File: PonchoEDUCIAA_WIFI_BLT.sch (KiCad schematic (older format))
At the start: 19 parts, among them J1 UART, U1 ESP32-WROOM

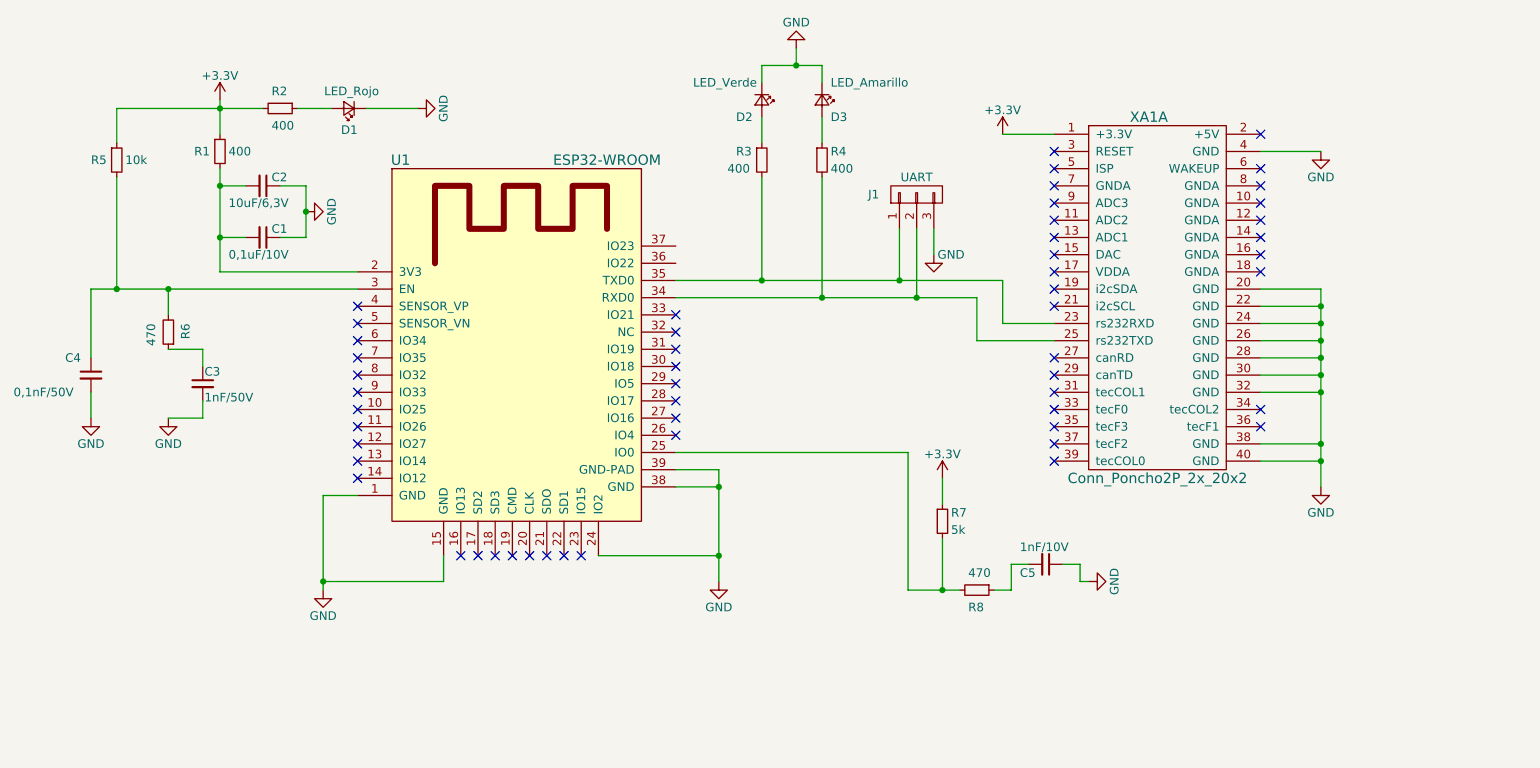
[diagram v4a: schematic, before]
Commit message: Se agregan switches al esquematico
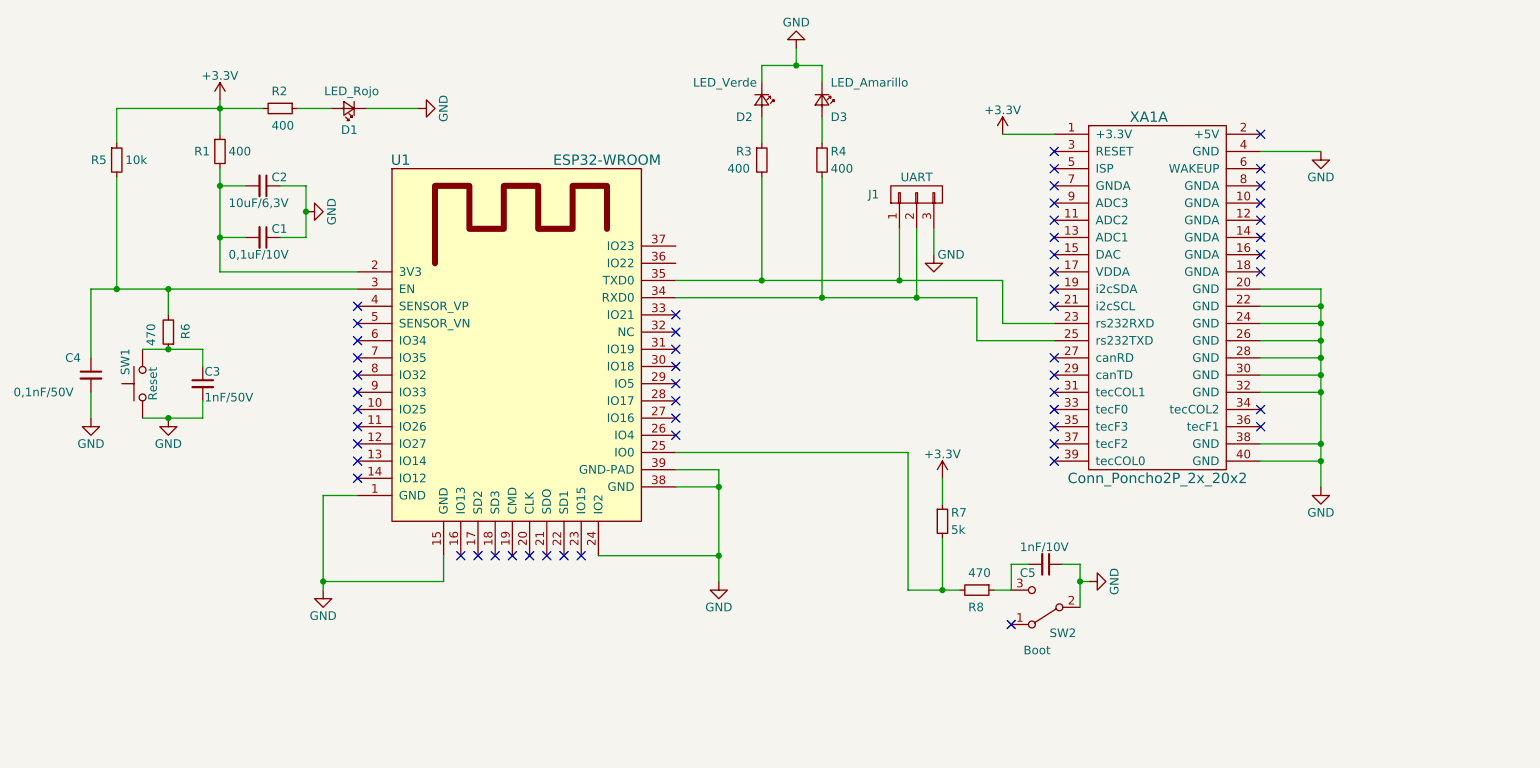
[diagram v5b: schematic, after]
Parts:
- added SW1: Reset, symbol SW_Push
- added SW2: Boot, symbol SW_SPDT
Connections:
- net GND: now also SW1.1, SW2.2 (B)
- net at C3.1, R6.1: now also SW1.2
- net at C5.2, R8.1: now also SW2.3 (C)
- no-connect marks 54 -> 55
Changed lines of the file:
@@
 LIBS:ej2cese
 LIBS:PonchoEDUCIAA_WIFI_BLT
+LIBS:switches
 LIBS:PonchoEDUCIAA_WIFI_BLT-cache
 EELAYER 25 0
@@
 	1    0    0    -1
 $EndComp
-Wire Wire Line
-	4450 5050 4450 5200
-Wire Wire Line
-	4450 5200 3750 5200
-Wire Wire Line
-	3950 4700 3750 4700
-Wire Wire Line
-	3750 4700 3750 5250
-Connection ~ 3750 5200
-Wire Wire Line
-	5800 4650 6050 4650
-Wire Wire Line
-	6050 4550 6050 5200
 $Comp
 L Conn_Poncho2P_2x_20x2 XA1
@@
 	1    0    0    -1
 $EndComp
-Wire Wire Line
-	5800 3550 7550 3550
-Wire Wire Line
-	7550 3550 7550 3800
-Wire Wire Line
-	7550 3800 8000 3800
-Wire Wire Line
-	5800 3450 7700 3450
-Wire Wire Line
-	7700 3450 7700 3700
-Wire Wire Line
-	7700 3700 8000 3700
 $Comp
 L R_Small R1
@@
 	1    0    0    -1
 $EndComp
-Wire Wire Line
-	3950 3400 3150 3400
-Wire Wire Line
-	3150 3400 3150 2800
-Wire Wire Line
-	3150 2400 3150 2600
 $Comp
 L R_Small R3
@@
 	0    1    1    0
 $EndComp
-Wire Wire Line
-	6300 2650 6300 2500
-Wire Wire Line
-	6300 2850 6300 3450
-Connection ~ 6300 3450
 $Comp
 L R_Small R4
@@
 	0    1    1    0
 $EndComp
-Wire Wire Line
-	6650 2650 6650 2500
-Wire Wire Line
-	6300 2300 6300 2200
-Wire Wire Line
-	6300 2200 6650 2200
-Wire Wire Line
-	6500 2200 6500 2100
-Wire Wire Line
-	6650 2200 6650 2300
-Connection ~ 6500 2200
 $Comp
 L R_Small R2
@@
 	0    -1   -1   0
 $EndComp
-Wire Wire Line
-	2550 2450 3400 2450
-Connection ~ 3150 2450
-Wire Wire Line
-	3600 2450 3800 2450
-Wire Wire Line
-	4000 2450 4300 2450
 $Comp
 L +3.3V #PWR?
@@
 	1    0    0    -1
 $EndComp
-Wire Wire Line
-	8000 2600 7700 2600
 $Comp
 L GND #PWR?
@@
 	1    0    0    -1
 $EndComp
-Wire Wire Line
-	9200 2700 9550 2700
 $Comp
 L GND #PWR?
@@
 	1    0    0    -1
 $EndComp
-Wire Wire Line
-	9200 3500 9550 3500
-Wire Wire Line
-	9550 3500 9550 4650
-Wire Wire Line
-	9200 3600 9550 3600
-Connection ~ 9550 3600
-Wire Wire Line
-	9200 3700 9550 3700
-Connection ~ 9550 3700
-Wire Wire Line
-	9200 3800 9550 3800
-Connection ~ 9550 3800
-Wire Wire Line
-	9200 3900 9550 3900
-Connection ~ 9550 3900
-Wire Wire Line
-	9200 4000 9550 4000
-Connection ~ 9550 4000
-Wire Wire Line
-	9200 4100 9550 4100
-Connection ~ 9550 4100
-Wire Wire Line
-	9200 4400 9550 4400
-Connection ~ 9550 4400
-Wire Wire Line
-	9200 4500 9550 4500
-Connection ~ 9550 4500
-Wire Wire Line
-	6650 2850 6650 3550
-Connection ~ 6650 3550
 $Comp
 L CONN_01X03 J1
@@
 	0    -1   -1   0
 $EndComp
-Wire Wire Line
-	7200 3150 7200 3550
-Connection ~ 7200 3550
-Wire Wire Line
-	7100 3150 7100 3450
-Connection ~ 7100 3450
 $Comp
 L GND #PWR?
@@
 	1    0    0    -1
 $EndComp
-Wire Wire Line
-	7300 3300 7300 3150
 $Comp
 L GND #PWR?
@@
 	0    -1   -1   0
 $EndComp
-Wire Wire Line
-	3500 2900 3650 2900
-Wire Wire Line
-	3650 2900 3650 3200
-Wire Wire Line
-	3650 3200 3500 3200
-Connection ~ 3650 3050
-Wire Wire Line
-	3300 2900 3150 2900
-Connection ~ 3150 2900
-Wire Wire Line
-	3300 3200 3150 3200
-Connection ~ 3150 3200
-Wire Wire Line
-	2400 3500 3950 3500
 $Comp
 L R_Small R6
@@
 	-1   0    0    1
 $EndComp
-Wire Wire Line
-	2850 3650 2850 3500
-Connection ~ 2850 3500
-Wire Wire Line
-	3050 3950 3050 3850
-Wire Wire Line
-	3050 3850 2850 3850
-Wire Wire Line
-	2850 4250 3050 4250
-Wire Wire Line
-	3050 4250 3050 4150
 $Comp
 L R_Small R5
@@
 	1    0    0    -1
 $EndComp
-Wire Wire Line
-	2550 2450 2550 2650
-Wire Wire Line
-	2550 3500 2550 2850
 $Comp
 L C_Small C4
@@
 	1    0    0    -1
 $EndComp
-Wire Wire Line
-	2400 3500 2400 3900
-Connection ~ 2550 3500
-Wire Wire Line
-	2400 4100 2400 4250
 NoConn ~ 3950 3600
 NoConn ~ 3950 3700
@@
 NoConn ~ 9200 4200
 NoConn ~ 9200 4300
-Wire Wire Line
-	5800 4450 7150 4450
-Wire Wire Line
-	7150 4450 7150 5250
 $Comp
 L GND #PWR?
@@
 	1    0    0    -1
 $EndComp
-Wire Wire Line
-	7150 5250 7450 5250
-Wire Wire Line
-	7350 5250 7350 4950
-Wire Wire Line
-	7350 4750 7350 4600
 $Comp
 L R_Small R8
@@
 	0    1    1    0
 $EndComp
-Connection ~ 7350 5250
-Wire Wire Line
-	7650 5250 7750 5250
-Wire Wire Line
-	7750 5250 7750 5100
-Wire Wire Line
-	7750 5100 7850 5100
-Wire Wire Line
-	8050 5100 8150 5100
-Wire Wire Line
-	8150 5100 8150 5200
-Wire Wire Line
-	8150 5200 8200 5200
 NoConn ~ 4950 5050
 NoConn ~ 4850 5050
@@
 NoConn ~ 4550 5050
 NoConn ~ 5250 5050
-Wire Wire Line
-	5350 5050 6050 5050
-Connection ~ 6050 5050
 NoConn ~ 5800 3650
 NoConn ~ 5800 3850
@@
 NoConn ~ 3950 4600
 Wire Wire Line
+	4450 5050 4450 5200
+Wire Wire Line
+	4450 5200 3750 5200
+Wire Wire Line
+	3950 4700 3750 4700
+Wire Wire Line
+	3750 4700 3750 5250
+Connection ~ 3750 5200
+Wire Wire Line
+	5800 4650 6050 4650
+Wire Wire Line
+	6050 4550 6050 5200
+Wire Wire Line
+	5800 3550 7550 3550
+Wire Wire Line
+	7550 3550 7550 3800
+Wire Wire Line
+	7550 3800 8000 3800
+Wire Wire Line
+	5800 3450 7700 3450
+Wire Wire Line
+	7700 3450 7700 3700
+Wire Wire Line
+	7700 3700 8000 3700
+Wire Wire Line
+	3950 3400 3150 3400
+Wire Wire Line
+	3150 3400 3150 2800
+Wire Wire Line
+	3150 2400 3150 2600
+Wire Wire Line
+	6300 2650 6300 2500
+Wire Wire Line
+	6300 2850 6300 3450
+Connection ~ 6300 3450
+Wire Wire Line
+	6650 2650 6650 2500
+Wire Wire Line
+	6300 2300 6300 2200
+Wire Wire Line
+	6300 2200 6650 2200
+Wire Wire Line
+	6500 2200 6500 2100
+Wire Wire Line
+	6650 2200 6650 2300
+Connection ~ 6500 2200
+Wire Wire Line
+	2550 2450 3400 2450
+Connection ~ 3150 2450
+Wire Wire Line
+	3600 2450 3800 2450
+Wire Wire Line
+	4000 2450 4300 2450
+Wire Wire Line
+	8000 2600 7700 2600
+Wire Wire Line
+	9200 2700 9550 2700
+Wire Wire Line
+	9200 3500 9550 3500
+Wire Wire Line
+	9550 3500 9550 4650
+Wire Wire Line
+	9200 3600 9550 3600
+Connection ~ 9550 3600
+Wire Wire Line
+	9200 3700 9550 3700
+Connection ~ 9550 3700
+Wire Wire Line
+	9200 3800 9550 3800
+Connection ~ 9550 3800
+Wire Wire Line
+	9200 3900 9550 3900
+Connection ~ 9550 3900
+Wire Wire Line
+	9200 4000 9550 4000
+Connection ~ 9550 4000
+Wire Wire Line
+	9200 4100 9550 4100
+Connection ~ 9550 4100
+Wire Wire Line
+	9200 4400 9550 4400
+Connection ~ 9550 4400
+Wire Wire Line
+	9200 4500 9550 4500
+Connection ~ 9550 4500
+Wire Wire Line
+	6650 2850 6650 3550
+Connection ~ 6650 3550
+Wire Wire Line
+	7200 3150 7200 3550
+Connection ~ 7200 3550
+Wire Wire Line
+	7100 3150 7100 3450
+Connection ~ 7100 3450
+Wire Wire Line
+	7300 3300 7300 3150
+Wire Wire Line
+	3500 2900 3650 2900
+Wire Wire Line
+	3650 2900 3650 3200
+Wire Wire Line
+	3650 3200 3500 3200
+Connection ~ 3650 3050
+Wire Wire Line
+	3300 2900 3150 2900
+Connection ~ 3150 2900
+Wire Wire Line
+	3300 3200 3150 3200
+Connection ~ 3150 3200
+Wire Wire Line
+	2400 3500 3950 3500
+Wire Wire Line
+	2850 3650 2850 3500
+Connection ~ 2850 3500
+Wire Wire Line
+	3050 3850 3050 3950
+Wire Wire Line
+	2700 3850 3050 3850
+Wire Wire Line
+	2700 4250 3050 4250
+Wire Wire Line
+	3050 4250 3050 4150
+Wire Wire Line
+	2550 2450 2550 2650
+Wire Wire Line
+	2550 3500 2550 2850
+Wire Wire Line
+	2400 3500 2400 3900
+Connection ~ 2550 3500
+Wire Wire Line
+	2400 4100 2400 4250
+Wire Wire Line
+	5800 4450 7150 4450
+Wire Wire Line
+	7150 4450 7150 5250
+Wire Wire Line
+	7150 5250 7450 5250
+Wire Wire Line
+	7350 5250 7350 4950
+Wire Wire Line
+	7350 4750 7350 4600
+Connection ~ 7350 5250
+Wire Wire Line
+	7650 5250 7750 5250
+Wire Wire Line
+	7750 5250 7750 5100
+Wire Wire Line
+	7750 5100 7850 5100
+Wire Wire Line
+	8050 5100 8150 5100
+Wire Wire Line
+	8150 5100 8150 5350
+Wire Wire Line
+	8150 5200 8200 5200
+Wire Wire Line
+	5350 5050 6050 5050
+Connection ~ 6050 5050
+Wire Wire Line
 	5800 4550 6050 4550
 Connection ~ 6050 4650
+$Comp
+L SW_Push SW1
+U 1 1 591BAB0F
+P 2700 4050
+F 0 "SW1" H 2750 4150 50  0000 L CNN
+F 1 "Reset" H 2700 3990 50  0000 C CNN
+F 2 "" H 2700 4250 50  0001 C CNN
+F 3 "" H 2700 4250 50  0001 C CNN
+	1    2700 4050
+	0    -1   -1   0
+$EndComp
+Connection ~ 2850 3850
+Connection ~ 2850 4250
+$Comp
+L SW_SPDT SW2
+U 1 1 591BBB9C
+P 7950 5350
+F 0 "SW2" H 7850 5500 50  0000 C CNN
+F 1 "Boot" H 8000 5600 50  0000 C CNN
+F 2 "" H 7950 5350 50  0001 C CNN
+F 3 "" H 7950 5350 50  0001 C CNN
+	1    7950 5350
+	-1   0    0    1
+$EndComp
+Connection ~ 8150 5200
+NoConn ~ 7750 5450
 $EndSCHEMATC

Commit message: Se agregan los footprints
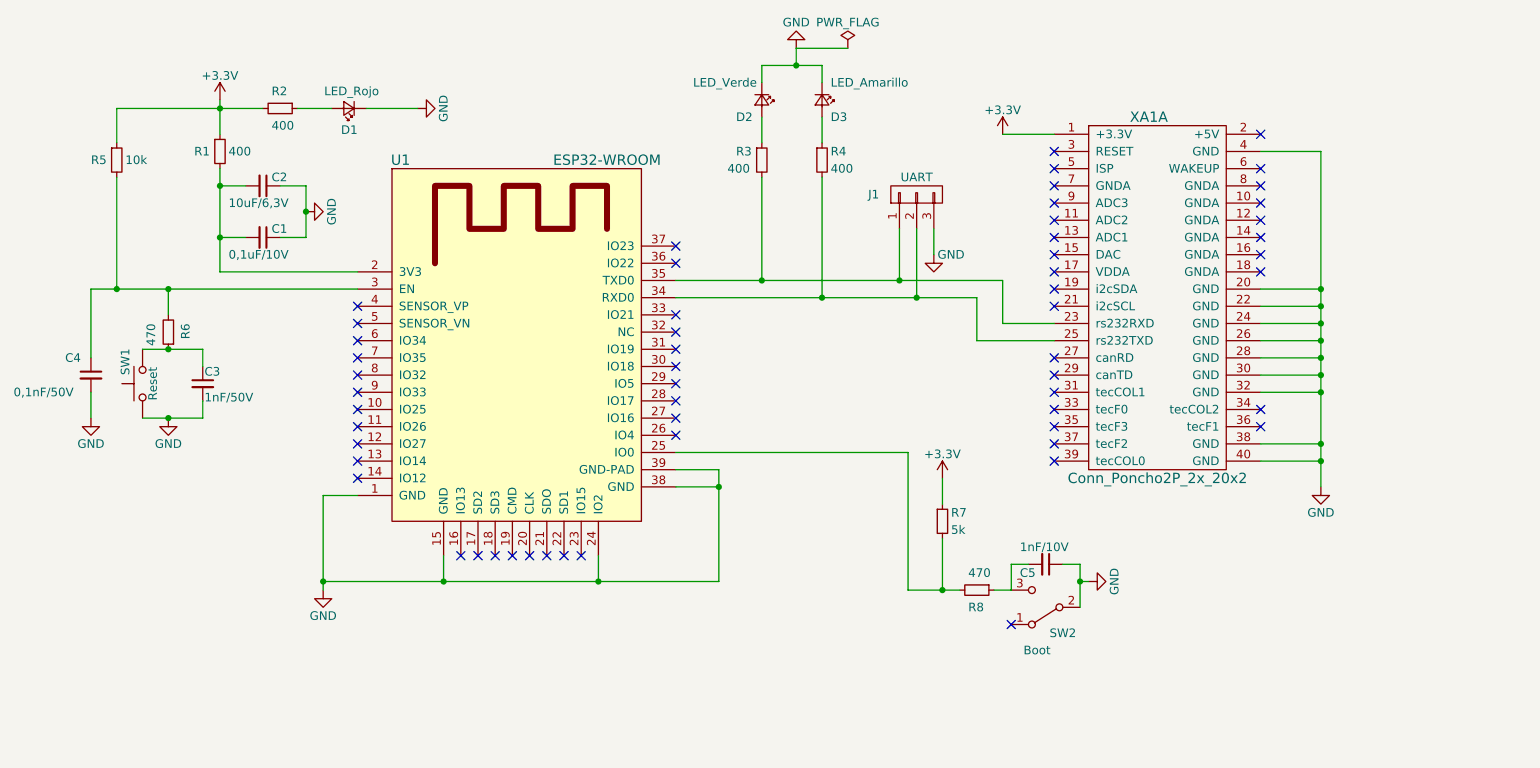
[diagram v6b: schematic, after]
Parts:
- C1, C2, C3, C4, C5: footprint (none) -> Capacitors_SMD:C_0603_HandSoldering
- D1, D2, D3: footprint (none) -> LEDs:LED_0402
- J1: footprint (none) -> PonchoEDUCIAA_WIFI_BLTH:CON_PALETA_3
- R1, R2, R3, R4, R5, R6, R7, R8: footprint (none) -> Resistors_SMD:R_1206_HandSoldering
- SW1: footprint (none) -> Buttons_Switches_ThroughHole:SW_PUSH_6mm
- SW2: footprint (none) -> Buttons_Switches_ThroughHole:SW_Micro_SPST
- XA1: footprint (none) -> PonchoEDUCIAA_WIFI_BLTH:Conn_Poncho_Derecha
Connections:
- no-connect marks 55 -> 57

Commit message: Se soluciona problema al importar netlist al pcbnew
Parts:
- SW1: footprint Buttons_Switches_ThroughHole:SW_PUSH_6mm -> Buttons_Switches_THT:SW_PUSH_6mm
- SW2: footprint Buttons_Switches_ThroughHole:SW_Micro_SPST -> Buttons_Switches_THT:SW_Micro_SPST
- U1: footprint PonchoEDUCIAA_WIFI_BLT:ESP32-WROOM -> PonchoEDUCIAA_WIFI_BLTH:ESP32-WROOM
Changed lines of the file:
@@
 LIBS:interface
 LIBS:ej2cese
-LIBS:PonchoEDUCIAA_WIFI_BLT
 LIBS:switches
+LIBS:PonchoEDUCIAA_WIFI_BLTH
 LIBS:PonchoEDUCIAA_WIFI_BLT-cache
 EELAYER 25 0
@@
 F 0 "U1" H 4200 5250 60  0000 C CNN
 F 1 "ESP32-WROOM" H 5400 5250 60  0000 C CNN
-F 2 "PonchoEDUCIAA_WIFI_BLT:ESP32-WROOM" H 5250 5350 60  0001 C CNN
+F 2 "PonchoEDUCIAA_WIFI_BLTH:ESP32-WROOM" H 5250 5350 60  0001 C CNN
 F 3 "" H 4450 4450 60  0001 C CNN
 	1    4900 4000
@@
 F 0 "SW1" H 2750 4150 50  0000 L CNN
 F 1 "Reset" H 2700 3990 50  0000 C CNN
-F 2 "Buttons_Switches_ThroughHole:SW_PUSH_6mm" H 2700 4250 50  0001 C CNN
+F 2 "Buttons_Switches_THT:SW_PUSH_6mm" H 2700 4250 50  0001 C CNN
 F 3 "" H 2700 4250 50  0001 C CNN
 	1    2700 4050
@@
 F 0 "SW2" H 7850 5500 50  0000 C CNN
 F 1 "Boot" H 8000 5600 50  0000 C CNN
-F 2 "Buttons_Switches_ThroughHole:SW_Micro_SPST" H 7950 5350 50  0001 C CNN
+F 2 "Buttons_Switches_THT:SW_Micro_SPST" H 7950 5350 50  0001 C CNN
 F 3 "" H 7950 5350 50  0001 C CNN
 	1    7950 5350
